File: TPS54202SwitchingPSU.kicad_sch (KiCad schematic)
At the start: 10 parts, among them CN1 Header_2_pin, CN2 Header_2_pin, U2 TPS54202DDC

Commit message: Rev A production release
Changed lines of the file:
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@@
+		)
+	)
+	(label "TPS54202 Switching PSU 8-25V in, 5V 2A out"
+		(at 195.58 190.5 0)
+		(effects
+			(font
+				(size 1.27 1.27)
+			)
+			(justify left bottom)
+		)
+	)
+	(label "A"
+		(at 270.51 194.31 0)
+		(effects
+			(font
+				(size 1.27 1.27)
+			)
+			(justify left bottom)
 		)
 	)

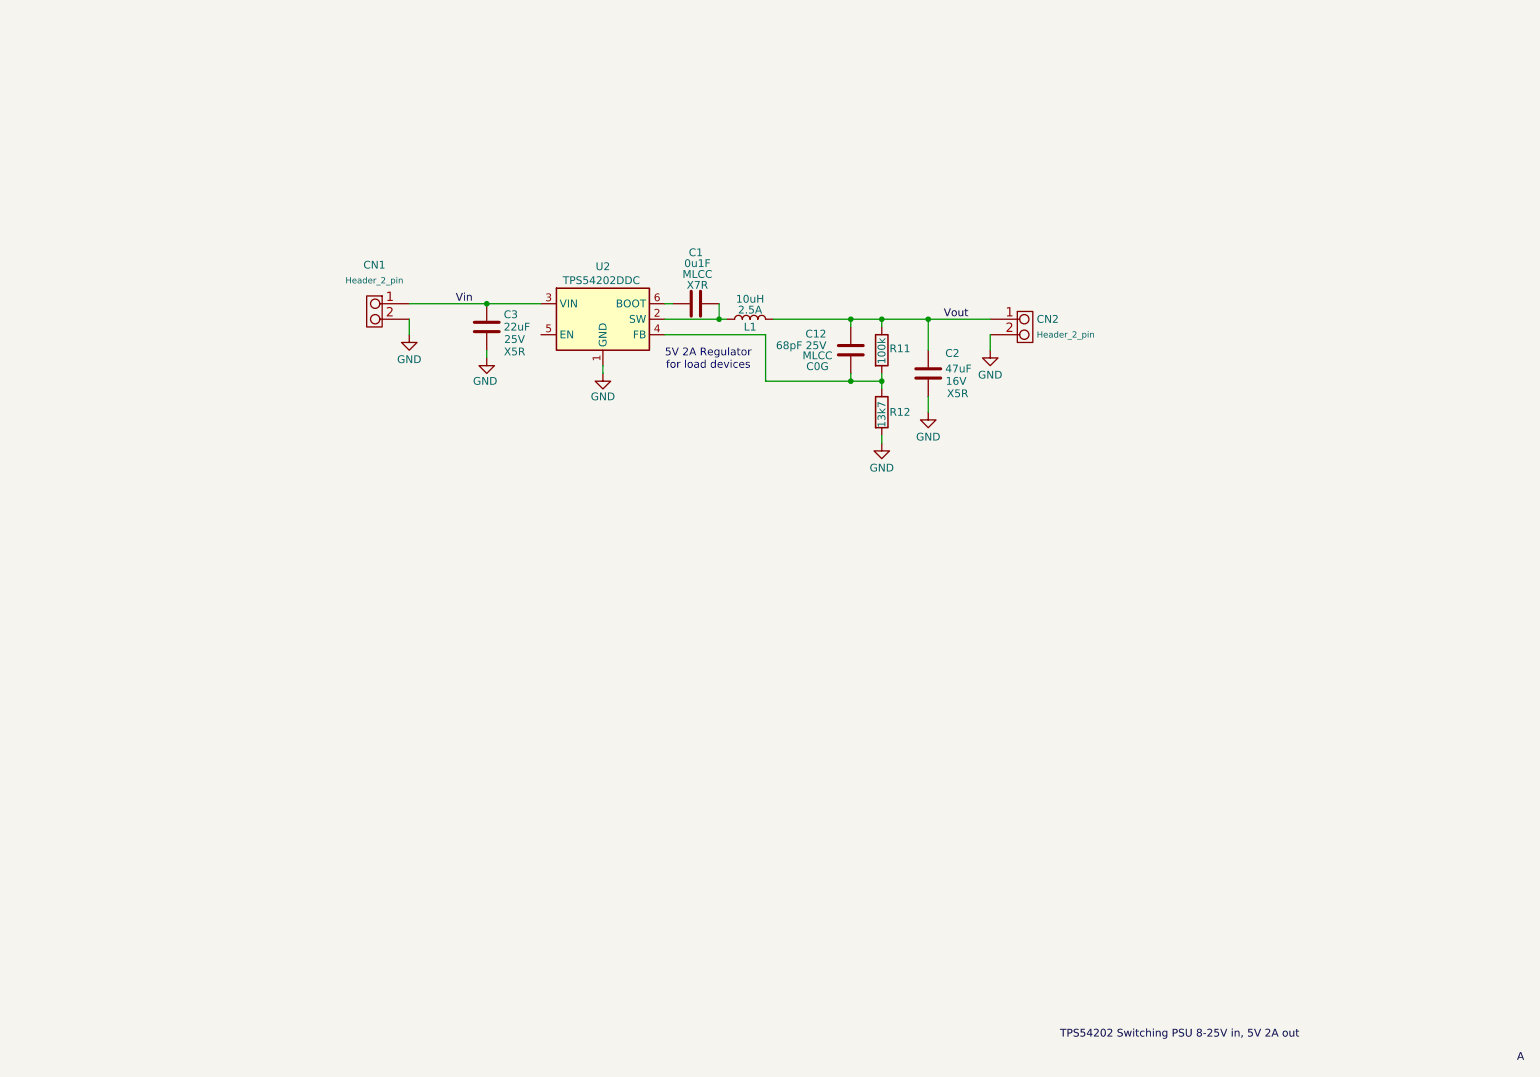
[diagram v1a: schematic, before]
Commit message: Updated to Rev B to fix board errors
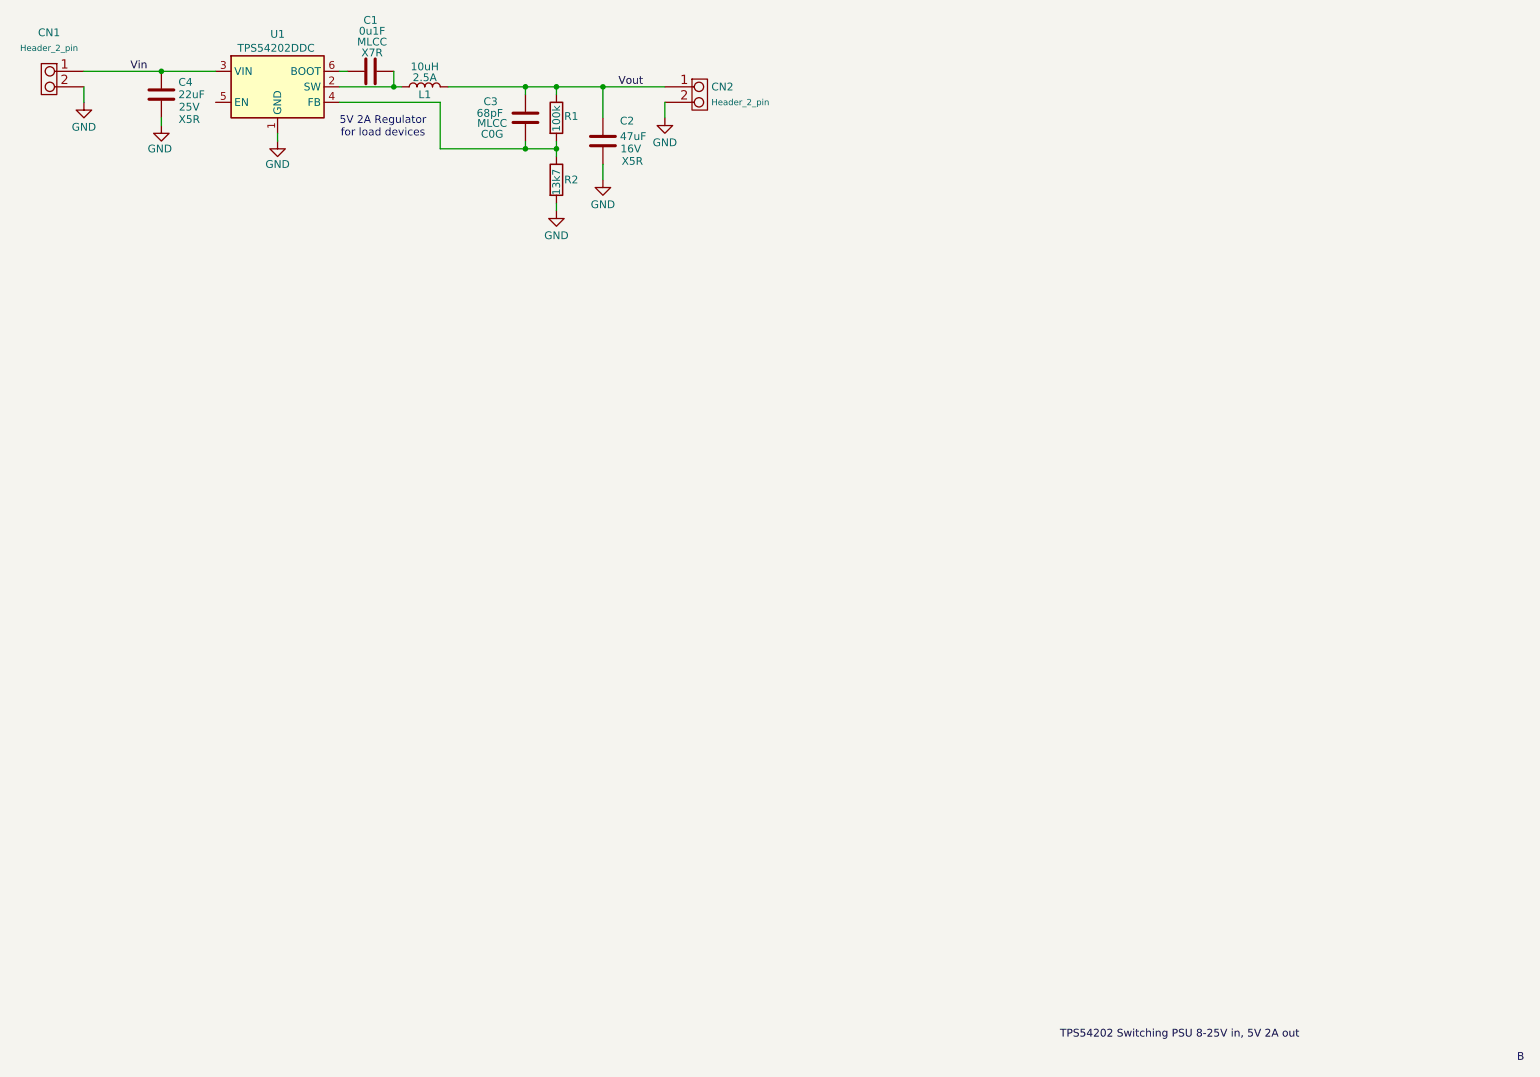
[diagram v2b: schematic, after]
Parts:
- C3: renamed from C12; value 68pF 25V -> 68pF; footprint Capacitor_SMD:C_0201_0603Metric_Pad0.64x0.40mm_HandSolder -> Capacitor_SMD:C_0805_2012Metric_Pad1.18x1.45mm_HandSolder; LCSC C2183472 -> C565680; Manuf Murata GRM0335C1E680GA01D -> PSA FV21N680J102ECG
- R1: renamed from R11; footprint Resistor_SMD:R_1206_3216Metric_Pad1.30x1.75mm_HandSolder -> Resistor_SMD:R_0805_2012Metric_Pad1.20x1.40mm_HandSolder
- R2: renamed from R12; footprint Resistor_SMD:R_1206_3216Metric_Pad1.30x1.75mm_HandSolder -> Resistor_SMD:R_0805_2012Metric_Pad1.20x1.40mm_HandSolder
- renumbered C3 to C4, U2 to U1
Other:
- moved on the sheet: C1, C2, C3, C4, CN1, CN2, L1, R1, R2, U1
